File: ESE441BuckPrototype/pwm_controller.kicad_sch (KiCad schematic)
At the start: 48 parts

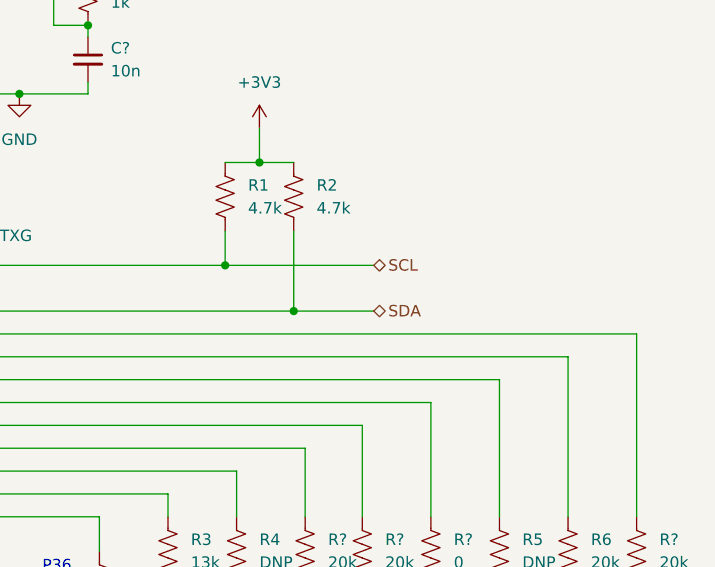
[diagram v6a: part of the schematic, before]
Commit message: Change I2C to bus
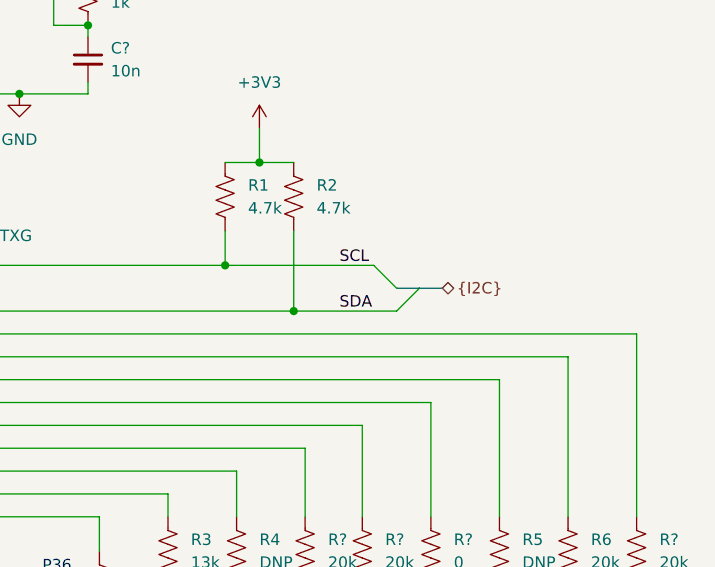
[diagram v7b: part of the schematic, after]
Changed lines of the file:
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@@
   (junction (at 142.24 41.91) (diameter 0) (color 0 0 0 0)
   )
+  (bus_entry (at 193.04 71.12) (size -2.54 -2.54)
+    (stroke (width 0) (type default) (color 0 0 0 0))
+  )
   (bus_entry (at 44.45 60.96) (size 2.54 2.54)
     (stroke (width 0) (type default) (color 0 0 0 0))
@@
     (stroke (width 0) (type default) (color 0 0 0 0))
   )
+  (bus_entry (at 195.58 71.12) (size -2.54 2.54)
+    (stroke (width 0) (type default) (color 0 0 0 0))
+  )
   (bus_entry (at 41.91 88.9) (size 2.54 2.54)
     (stroke (width 0) (type default) (color 0 0 0 0))
@@
     (stroke (width 0) (type default) (color 0 0 0 0))
   )
+  (bus (pts (xy 195.58 71.12) (xy 198.12 71.12))
+    (stroke (width 0) (type default) (color 0 0 0 0))
+  )
   (wire (pts (xy 125.73 121.92) (xy 125.73 142.24))
     (stroke (width 0) (type default) (color 0 0 0 0))
@@
     (stroke (width 0) (type default) (color 0 0 0 0))
   )
+  (bus (pts (xy 193.04 71.12) (xy 195.58 71.12))
+    (stroke (width 0) (type default) (color 0 0 0 0))
+  )
   (wire (pts (xy 182.88 88.9) (xy 140.97 88.9))
     (stroke (width 0) (type default) (color 0 0 0 0))
@@
     (stroke (width 0) (type default) (color 0 0 0 0))
   )
-  (wire (pts (xy 181.61 73.66) (xy 190.5 73.66))
+  (wire (pts (xy 181.61 73.66) (xy 193.04 73.66))
     (stroke (width 0) (type default) (color 0 0 0 0))
   )
@@
     (effects (font (size 1.27 1.27)) (justify right bottom))
   )
+  (label "SDA" (at 186.69 73.66 0)
+    (effects (font (size 1.27 1.27)) (justify left bottom))
+  )
   (label "PH1.PWM" (at 102.87 46.99 90)
     (effects (font (size 1.27 1.27)) (justify left bottom))
@@
     (effects (font (size 1.27 1.27)) (justify right bottom))
   )
+  (label "SCL" (at 186.69 68.58 0)
+    (effects (font (size 1.27 1.27)) (justify left bottom))
+  )
   (label "PH3.ISN" (at 46.99 91.44 270)
     (effects (font (size 1.27 1.27)) (justify right bottom))
@@
     (effects (font (size 1.27 1.27)) (justify right))
   )
-  (hierarchical_label "SCL" (shape bidirectional) (at 190.5 68.58 0)
-    (effects (font (size 1.27 1.27)) (justify left))
-  )
   (hierarchical_label "PGOOD" (shape input) (at 137.16 49.53 0)
     (effects (font (size 1.27 1.27)) (justify left))
@@
     (effects (font (size 1.27 1.27)) (justify left))
   )
+  (hierarchical_label "{I2C}" (shape bidirectional) (at 198.12 71.12 0)
+    (effects (font (size 1.27 1.27)) (justify left))
+  )
   (hierarchical_label "PH3{PH}" (shape bidirectional) (at 34.29 88.9 180)
     (effects (font (size 1.27 1.27)) (justify right))
   )
-  (hierarchical_label "SDA" (shape bidirectional) (at 190.5 73.66 0)
-    (effects (font (size 1.27 1.27)) (justify left))
-  )
   (symbol (lib_id "power:VCC") (at 52.07 24.13 0) (unit 1)

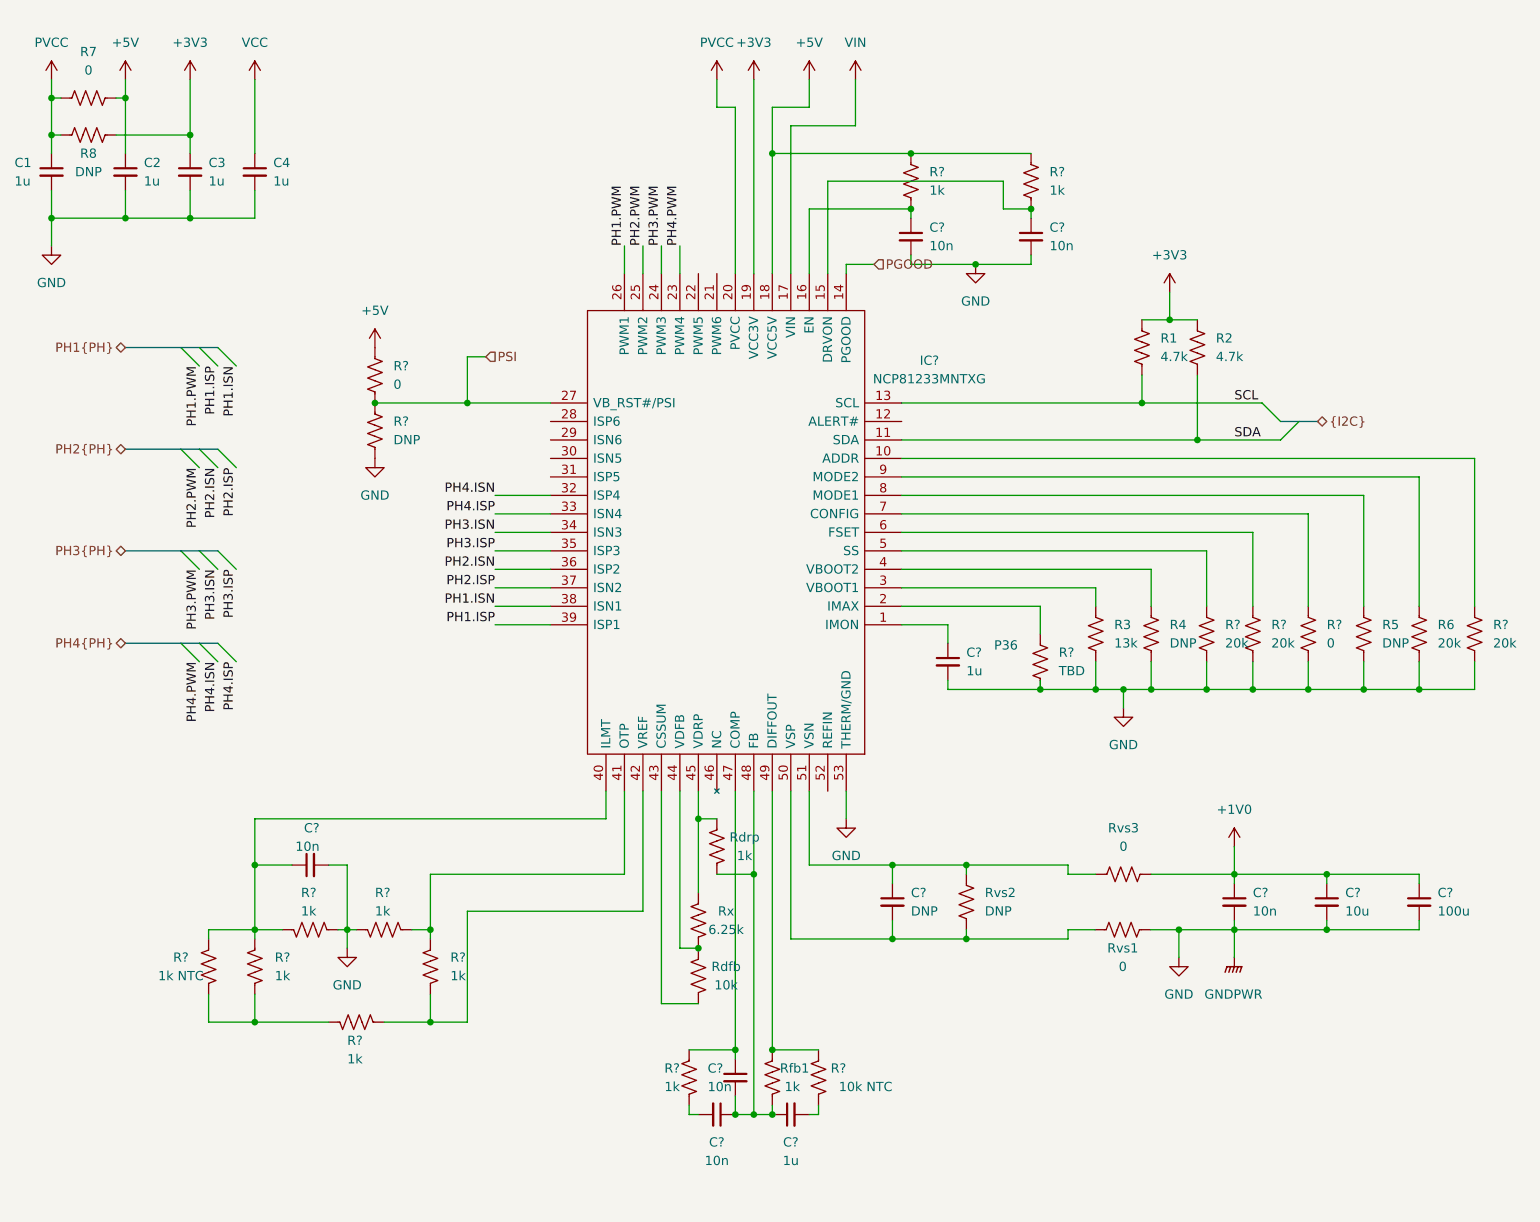
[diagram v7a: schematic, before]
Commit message: Add component names, values, PWM jumper
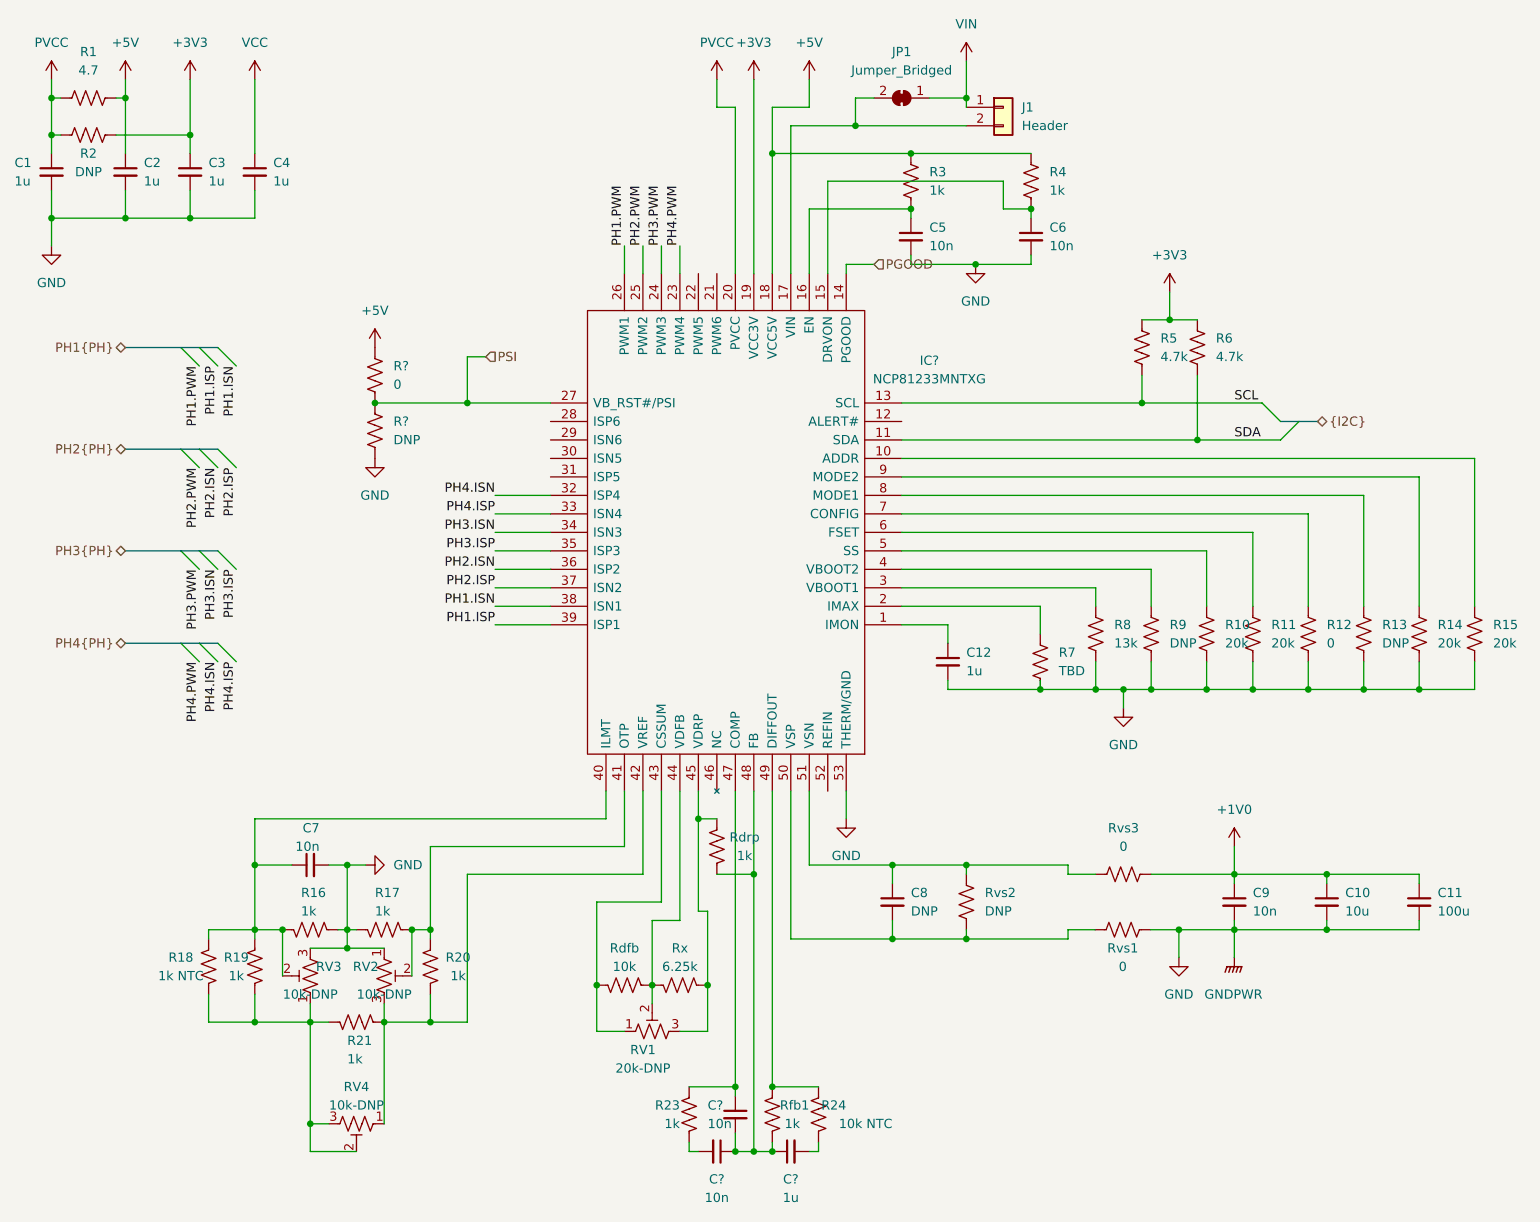
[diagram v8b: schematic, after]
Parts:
- added J1: Header, symbol Connector_Generic:Conn_01x02
- added JP1: Jumper_Bridged, symbol Jumper:SolderJumper_2_Bridged
- added RV1: 20k-DNP, symbol Device:R_Potentiometer_Trim_US
- added RV2, RV3, RV4: 10k-DNP, symbol Device:R_Potentiometer_Trim_US
- R1: renamed from R7; value 0 -> 4.7
- gave numbers to parts that had none: 23
- renumbered R5 to R13, R6 to R14, R8 to R2, R1 to R5, R2 to R6, R3 to R8, R4 to R9
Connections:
- net GND: now also RV2.1, RV3.3
- net VIN: now also J1.1 (Pin_1), JP1.1 (A); no longer IC?.17 (VIN)
- net at IC?.43 (CSSUM), Rdfb.1: now also RV1.1
- net at IC?.44 (VDFB), Rdfb.2: now also Rx.2, RV1.2; no longer Rx.1
- net at IC?.45 (VDRP), Rdrp.2: now also Rx.1, RV1.3; no longer Rx.2
- net at IC?.42 (VREF), R20.1, R21.1: now also RV2.3, RV4.1
- net at R18.1, R19.1, R21.2: now also RV3.1, RV4.2, RV4.3
- net at C7.1, IC?.40 (ILMT), R16.2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: now also RV3.2
- net at IC?.41 (OTP), R17.1, R20.2: now also RV2.2
- new net: IC?.17 (VIN), J1.2 (Pin_2), JP1.2 (B)
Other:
- note removed: "P36"
- moved on the sheet: C?, R23, R24, Rdfb, Rfb1, Rx
